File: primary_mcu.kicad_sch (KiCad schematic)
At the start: 44 parts, among them J1 Conn_ST_STDC14, J2 USB_C_Receptacle, SW1 SW_Wuerth_450301014042, SW2 SW_Omron_B3U-1000P, SW3 SW_Omron_B3U-1000P, U6 W25Q256JV, U7 STM32U575RGT6, U8 USBLC6-2P6, Y1 Q13MC14620002, Y2 ECS-TXO-2520MV

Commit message: PCB routing
- addition of 3D models
- addition of docs
- reduction of the size of passives
- increase in size of traces
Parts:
- C11, C12, C13, C14, C15, C16, C17, C19, C20, C22, C25: footprint Capacitor_SMD:C_0603_1608Metric -> Capacitor_SMD:C_0402_1005Metric
- R14, R15, R16, R17: footprint Resistor_SMD:R_0603_1608Metric -> Resistor_SMD:R_0402_1005Metric
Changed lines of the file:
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@@
 			)
 		)
-		(property "Footprint" "Capacitor_SMD:C_0603_1608Metric"
+		(property "Footprint" "Capacitor_SMD:C_0402_1005Metric"
 			(at 244.8052 110.49 0)
 			(effects
@@
 			)
 		)
-		(property "Footprint" "Resistor_SMD:R_0603_1608Metric"
+		(property "Footprint" "Resistor_SMD:R_0402_1005Metric"
 			(at 375.412 100.33 90)
 			(effects
@@
 			)
 		)
-		(property "Footprint" "Resistor_SMD:R_0603_1608Metric"
+		(property "Footprint" "Resistor_SMD:R_0402_1005Metric"
 			(at 75.692 214.63 90)
 			(effects
@@
 			)
 		)
-		(property "Footprint" "Resistor_SMD:R_0603_1608Metric"
+		(property "Footprint" "Resistor_SMD:R_0402_1005Metric"
 			(at 365.252 100.33 90)
 			(effects
@@
 			)
 		)
-		(property "Footprint" "Resistor_SMD:R_0603_1608Metric"
+		(property "Footprint" "Resistor_SMD:R_0402_1005Metric"
 			(at 168.91 185.928 90)
 			(effects
@@
 			)
 		)
-		(property "Footprint" "Capacitor_SMD:C_0603_1608Metric"
+		(property "Footprint" "Capacitor_SMD:C_0402_1005Metric"
 			(at 178.7652 120.65 0)
 			(effects
@@
 			)
 		)
-		(property "Footprint" "Capacitor_SMD:C_0603_1608Metric"
+		(property "Footprint" "Capacitor_SMD:C_0402_1005Metric"
 			(at 44.1452 215.9 0)
 			(effects
@@
 			)
 		)
-		(property "Footprint" "Capacitor_SMD:C_0603_1608Metric"
+		(property "Footprint" "Capacitor_SMD:C_0402_1005Metric"
 			(at 191.4652 48.26 0)
 			(effects
@@
 			)
 		)
-		(property "Footprint" "Capacitor_SMD:C_0603_1608Metric"
+		(property "Footprint" "Capacitor_SMD:C_0402_1005Metric"
 			(at 242.2652 48.26 0)
 			(effects
@@
 			)
 		)
-		(property "Footprint" "Capacitor_SMD:C_0603_1608Metric"
+		(property "Footprint" "Capacitor_SMD:C_0402_1005Metric"
 			(at 166.0652 48.26 0)
 			(effects
@@
 			)
 		)
-		(property "Footprint" "Capacitor_SMD:C_0603_1608Metric"
+		(property "Footprint" "Capacitor_SMD:C_0402_1005Metric"
 			(at 353.06 200.9648 0)
 			(effects
@@
 			)
 		)
-		(property "Footprint" "Capacitor_SMD:C_0603_1608Metric"
+		(property "Footprint" "Capacitor_SMD:C_0402_1005Metric"
 			(at 178.7652 48.26 0)
 			(effects
@@
 			)
 		)
-		(property "Footprint" "Capacitor_SMD:C_0603_1608Metric"
+		(property "Footprint" "Capacitor_SMD:C_0402_1005Metric"
 			(at 270.51 245.4148 0)
 			(effects
@@
 			)
 		)
-		(property "Footprint" "Capacitor_SMD:C_0603_1608Metric"
+		(property "Footprint" "Capacitor_SMD:C_0402_1005Metric"
 			(at 204.1652 120.65 0)
 			(effects
@@
 			)
 		)
-		(property "Footprint" "Capacitor_SMD:C_0603_1608Metric"
+		(property "Footprint" "Capacitor_SMD:C_0402_1005Metric"
 			(at 204.1652 48.26 0)
 			(effects

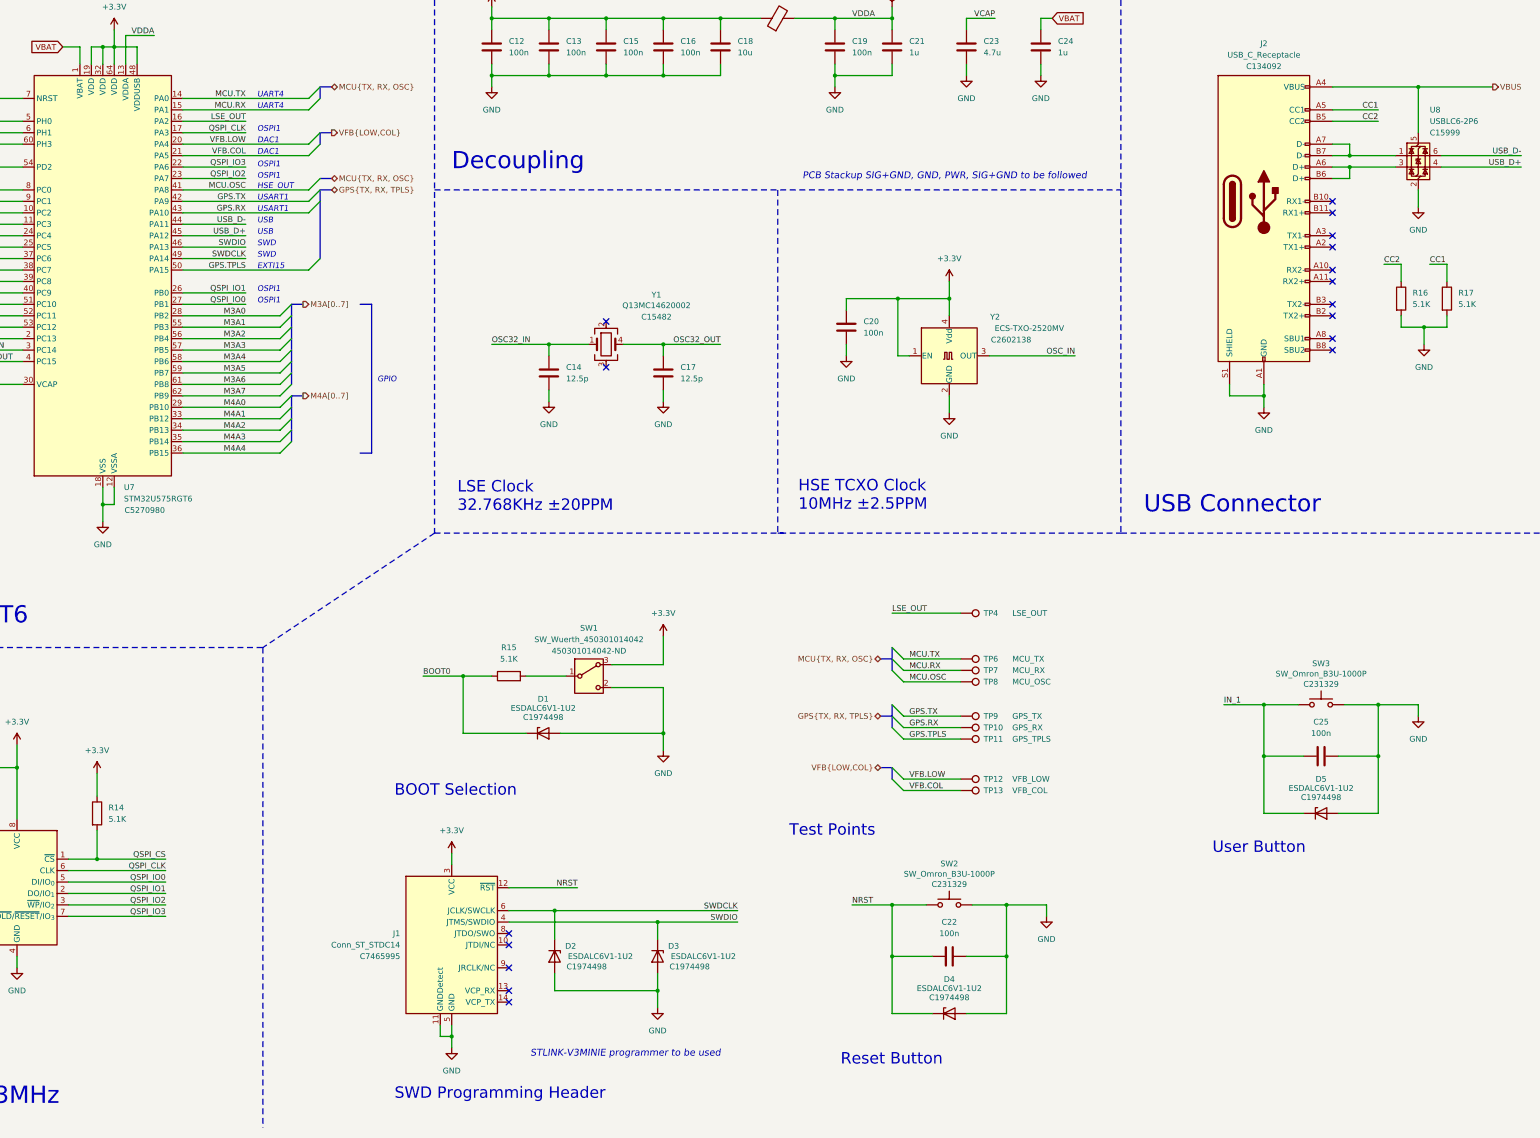
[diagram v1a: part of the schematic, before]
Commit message: PCB routing restarted
- removal of all previous traces and vias
- placement of most of the parts
- priority towards high speed lines like USB and USART
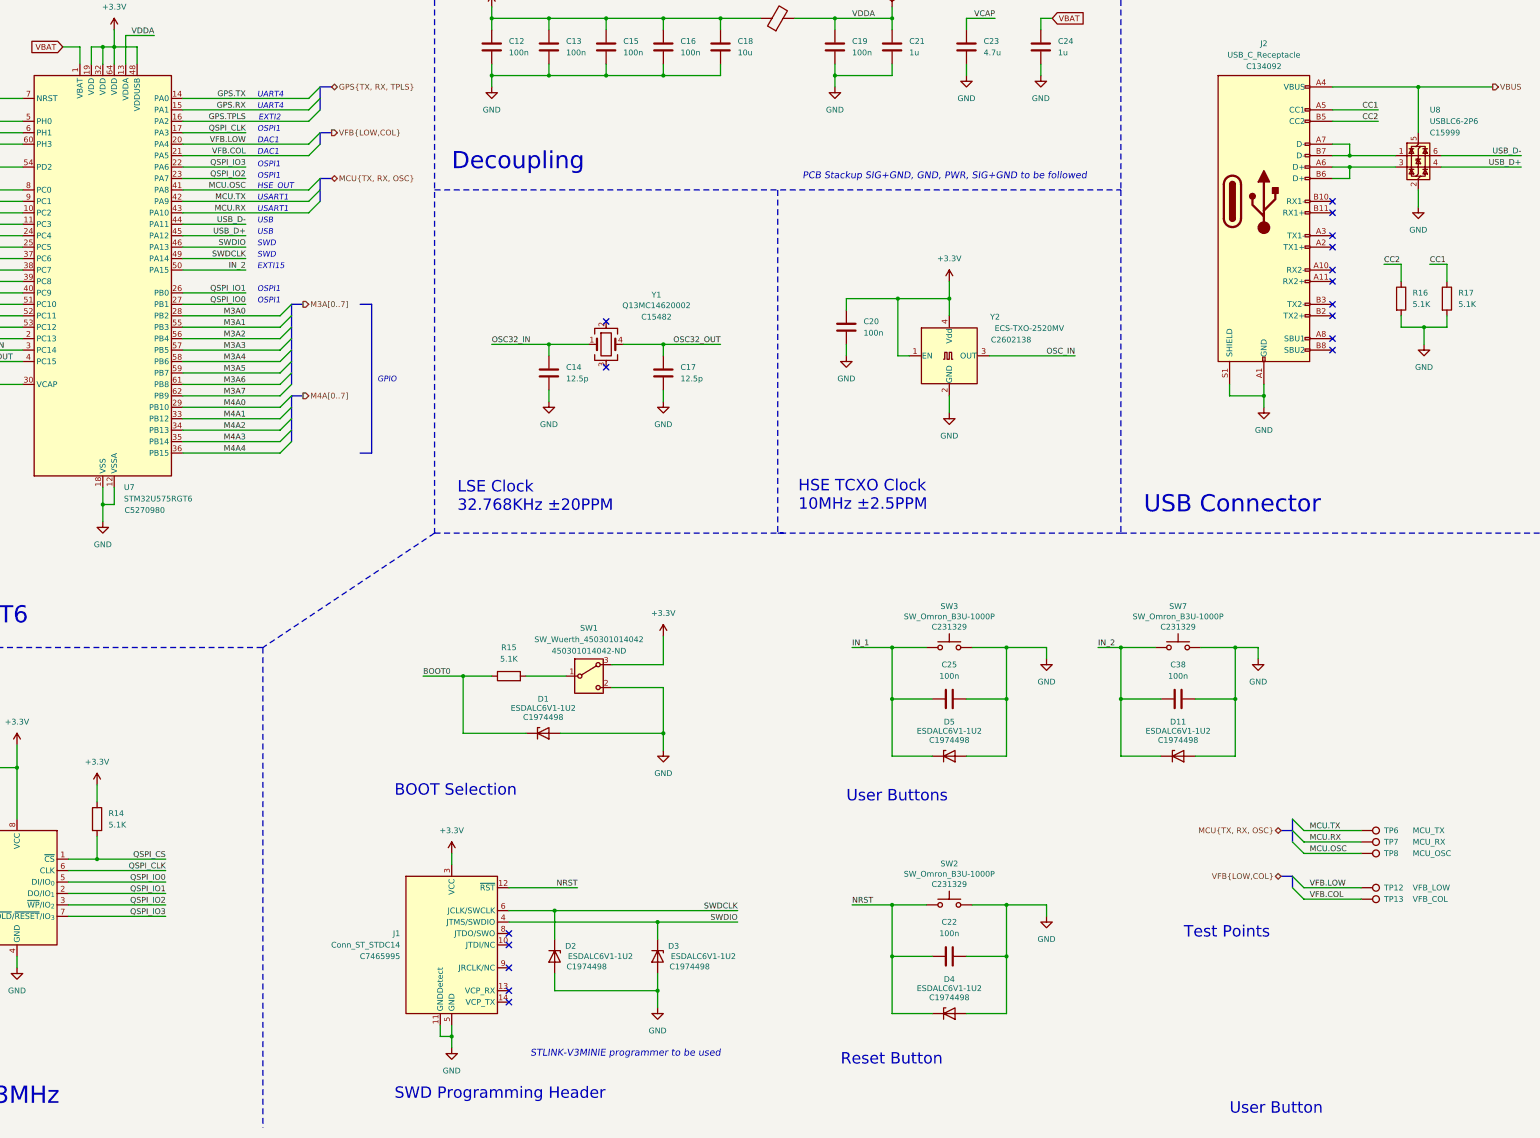
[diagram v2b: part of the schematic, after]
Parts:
- removed TP10: GPS_RX, TestPoint:TestPoint_Pad_D1.0mm, symbol Connector:TestPoint
- removed TP11: GPS_TPLS, TestPoint:TestPoint_Pad_D1.0mm, symbol Connector:TestPoint
- removed TP4: LSE_OUT, TestPoint:TestPoint_Pad_D1.0mm, symbol Connector:TestPoint
- removed TP9: GPS_TX, TestPoint:TestPoint_Pad_D1.0mm, symbol Connector:TestPoint
- added C38: 100n, Capacitor_SMD:C_0402_1005Metric, symbol Device:C
- added D11: ESDALC6V1-1U2, precision_clock:ST ESDALC6V1-1U2, symbol Diode:ESD5Zxx
- added SW7: SW_Omron_B3U-1000P, Button_Switch_SMD:SW_SPST_Omron_B3FS-100xP, symbol Switch:SW_Omron_B3FS
- C21, C24: footprint Capacitor_SMD:C_0603_1608Metric -> Capacitor_SMD:C_0402_1005Metric
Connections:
- net LSE_OUT is gone; now on net GPS.TPLS: U7.16 (PA2)
- net GND: now also C38.2, D11.2 (A), SW7.2
- net GPS.RX: now also U7.15 (PA1); no longer U7.43 (PA10)
- net GPS.TPLS: no longer U7.50 (PA15)
- net GPS.TX: now also U7.14 (PA0); no longer U7.42 (PA9)
- net MCU.RX: now also U7.43 (PA10); no longer U7.15 (PA1)
- net MCU.TX: now also U7.42 (PA9); no longer U7.14 (PA0)
- new net IN_2: C38.1, D11.1 (K), SW7.1, U7.50 (PA15)
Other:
- note added: "EXTI2"
- note added: "User Buttons"
- moved on the sheet: C25, D5, R14, SW3, TP12, TP13, TP6, TP7, TP8

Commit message: Major overhaul required
- Secondary MCU External clock to be included
- possible removal of colon drivers
- priority towards the end product over schematic
- high speed signals to be tuned like QSPI and USB
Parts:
- J2: footprint Connector_USB:USB_C_Receptacle_Molex_105450-0101 -> precision_clock:USB_C_Receptacle_Molex_105450-0101
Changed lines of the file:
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@@
 			)
 		)
-		(property "Footprint" "Connector_USB:USB_C_Receptacle_Molex_105450-0101"
+		(property "Footprint" "precision_clock:USB_C_Receptacle_Molex_105450-0101"
 			(at 340.36 78.74 0)
 			(effects

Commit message: Primary MCU rerouting
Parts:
- removed C38: 100n, Capacitor_SMD:C_0402_1005Metric, symbol Device:C
- removed D11, D2: ESDALC6V1-1U2, precision_clock:ST ESDALC6V1-1U2, symbol Diode:ESD5Zxx
- removed SW7: SW_Omron_B3U-1000P, Button_Switch_SMD:SW_SPST_Omron_B3FS-100xP, symbol Switch:SW_Omron_B3FS
- removed TP12: VFB_LOW, TestPoint:TestPoint_Pad_D1.0mm, symbol Connector:TestPoint
- removed TP13: VFB_COL, TestPoint:TestPoint_Pad_D1.0mm, symbol Connector:TestPoint
- added D4, D5, D6: ESDALC6V1-1U2, precision_clock:ST ESDALC6V1-1U2, symbol Diode:ESD5Zxx
- renumbered C25 to C22, C22 to C25, D5 to D2, D4 to D7, SW3 to SW2, SW2 to SW3, TP6 to TP4, TP7 to TP5, TP8 to TP6
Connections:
- net IN_2 is gone; now on net IN: U7.50 (PA15)
- net VFB.COL is gone; now on net USART_RX: U7.21 (PA5)
- net VFB.LOW is gone; now on net QSPI_CS: U7.20 (PA4)
- net COL0: now also U7.8 (PC0); no longer U7.53 (PC12)
- net COL1: now also U7.9 (PC1); no longer U7.2 (PC13)
- net GND: now also D4.2 (A), D5.2 (A), D6.2 (A)
- net M3A0: now also U7.51 (PC10); no longer U7.28 (PB2)
- net M3A1: now also U7.52 (PC11); no longer U7.55 (PB3)
- net M3A2: now also U7.53 (PC12); no longer U7.56 (PB4)
- net M3A3: now also U7.54 (PD2); no longer U7.57 (PB5)
- net M3A5: now also U7.57 (PB5); no longer U7.59 (PB7)
- net M3A6: now also U7.56 (PB4); no longer U7.61 (PB8)
- net M3A7: now also U7.55 (PB3); no longer U7.62 (PB9)
- net M3K0: now also U7.2 (PC13); no longer U7.10 (PC2)
- net M3K1: now also U7.62 (PB9); no longer U7.11 (PC3)
- net M3K2: now also U7.61 (PB8); no longer U7.24 (PC4)
- net M3K3: now also U7.59 (PB7); no longer U7.25 (PC5)
- net M4A0: now also U7.33 (PB12); no longer U7.29 (PB10)
- net M4A1: now also U7.34 (PB13); no longer U7.33 (PB12)
- net M4A2: now also U7.35 (PB14); no longer U7.34 (PB13)
- net M4A3: now also U7.36 (PB15); no longer U7.35 (PB14)
- net M4A4: now also U7.40 (PC9); no longer U7.36 (PB15)
- net M4A5: now also U7.39 (PC8); no longer U7.54 (PD2)
- net M4A6: now also U7.38 (PC7); no longer U7.8 (PC0)
- net M4A7: now also U7.37 (PC6); no longer U7.9 (PC1)
- net M4K0: now also U7.29 (PB10); no longer U7.37 (PC6)
- net M4K1: now also U7.28 (PB2); no longer U7.38 (PC7)
- net M4K2: now also U7.25 (PC5); no longer U7.39 (PC8)
- net M4K3: now also U7.11 (PC3); no longer U7.40 (PC9)
- net M4K4: now also U7.10 (PC2); no longer U7.51 (PC10)
- net QSPI_CS: no longer U7.52 (PC11)
- net SWDCLK: now also D4.1 (K)
- net USART_RX: now reaches J1.13 (VCP_RX)
- net USART_RX: now also D6.1 (K)
- net USART_TX: now reaches J1.14 (VCP_TX)
- net USART_TX: now also U7.24 (PC4), D5.1 (K)
- net IN_1 renamed IN
- net IN: no longer U7.6 (PH1)
- no-connect marks 17 -> 16
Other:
- note added: "ESD Protection"
- note added: "USART3"
- note removed: "DAC1"
- note removed: "EXTI1"
- note removed: "User Buttons"
- moved on the sheet: C25, D1, D7, J1, R15, SW1, SW3, TP4, TP5, TP6

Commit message: Secondary MCU rerouting
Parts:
- renumbered FB3 to FB2, TP4 to TP3, TP5 to TP4, TP6 to TP5
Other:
- note added: "Boot Switch to be replaced with SMD switch"
- moved on the sheet: C22, C25, D1, D2, D3, D4, D5, D6, D7, J1, R15, SW1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

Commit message: Secondary MCU complete
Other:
- note removed: "GPIO"
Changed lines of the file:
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@@
 		)
 	)
-	(text "GPIO"
-		(exclude_from_sim no)
-		(at 139.7 118.364 0)
-		(effects
-			(font
-				(size 1.27 1.27)
-				(italic yes)
-				(color 132 0 0 1)
-			)
-			(justify left)
-		)
-	)
 	(text "RCC32"
 		(exclude_from_sim no)
@@
 		)
 	)
-	(text "GPIO"
-		(exclude_from_sim no)
-		(at 20.32 88.9 0)
-		(effects
-			(font
-				(size 1.27 1.27)
-				(italic yes)
-				(color 132 0 0 1)
-			)
-			(justify right)
-		)
-	)
 	(text "USART3"
 		(exclude_from_sim no)
@@
 		)
 	)
-	(polyline
-		(pts
-			(xy 138.43 101.6) (xy 138.43 134.62)
-		)
-		(stroke
-			(width 0)
-			(type solid)
-			(color 132 0 0 1)
-		)
-	)
 	(wire
 		(pts
@@
 		)
 	)
-	(polyline
-		(pts
-			(xy 24.13 68.58) (xy 21.59 68.58)
-		)
-		(stroke
-			(width 0)
-			(type solid)
-			(color 132 0 0 1)
-		)
-	)
 	(wire
 		(pts
@@
 		)
 	)
-	(polyline
-		(pts
-			(xy 21.59 68.58) (xy 21.59 109.22)
-		)
-		(stroke
-			(width 0)
-			(type solid)
-			(color 132 0 0 1)
-		)
-	)
 	(wire
 		(pts
@@
 		)
 	)
-	(polyline
-		(pts
-			(xy 135.89 101.6) (xy 138.43 101.6)
-		)
-		(stroke
-			(width 0)
-			(type solid)
-			(color 132 0 0 1)
-		)
-	)
 	(wire
 		(pts
@@
 		)
 	)
-	(polyline
-		(pts
-			(xy 21.59 109.22) (xy 24.13 109.22)
-		)
-		(stroke
-			(width 0)
-			(type solid)
-			(color 132 0 0 1)
-		)
-	)
 	(wire
 		(pts
@@
 		)
 	)
-	(polyline
-		(pts
-			(xy 135.89 134.62) (xy 138.43 134.62)
-		)
-		(stroke
-			(width 0)
-			(type solid)
-			(color 132 0 0 1)
-		)
-	)

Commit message: PCB routing
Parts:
- removed SW1: SW_Wuerth_450301014042, Button_Switch_THT:SW_Slide-03_Wuerth-WS-SLTV_10x2.5x6.4_P2.54mm, symbol Switch:SW_Wuerth_450301014042
- added SW1: SW_ALPSALPINE, precision_clock:SW_ALPSALPINE, symbol precision_clock:SW_ALPSALPINE
- renumbered C11 to C13, C12 to C14, C13 to C15, C14 to C16, C15 to C17, C16 to C18, C17 to C19, C18 to C20, C19 to C21, C20 to C22, C21 to C23, C22 to C24, C23 to C25, C24 to C26, C25 to C27, TP3 to TP4, TP4 to TP5, TP5 to TP6
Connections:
- net +3.3V: now also SW1.1 (A)
- net GND: now also SW1.3 (B), SW1.4 (GND)
- net at R15.2: now also SW1.2 (C)
- net VBUS renamed VB
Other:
- note removed: "Boot Switch to be replaced with SMD switch"
- moved on the sheet: D1

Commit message: Schematic changes
- signal for dots are removed.
- power supply upgraded to buck converters.
- individually addressable Colon LEDs.
- second millisecond dot separator signal is not connected.
- buzzer can now be connected to PWM or DAC outputs.
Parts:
- renumbered C13 to C10, C14 to C11, C15 to C12, C16 to C13, C17 to C14, C18 to C15, C19 to C16, C20 to C17, C21 to C18, C22 to C19, C23 to C20, C24 to C21, C25 to C22, C26 to C23, C27 to C24, FB2 to FB1, R17 to R10, R14 to R7, R15 to R8, R16 to R9, TP4 to TP1, TP5 to TP2, TP6 to TP3, U6 to U4, U7 to U5, U8 to U6
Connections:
- net M3A7 renamed COL3
- net M4A7 renamed COL2
- net VB renamed VBUS
